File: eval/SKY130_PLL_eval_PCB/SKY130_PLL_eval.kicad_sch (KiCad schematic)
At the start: 0 parts

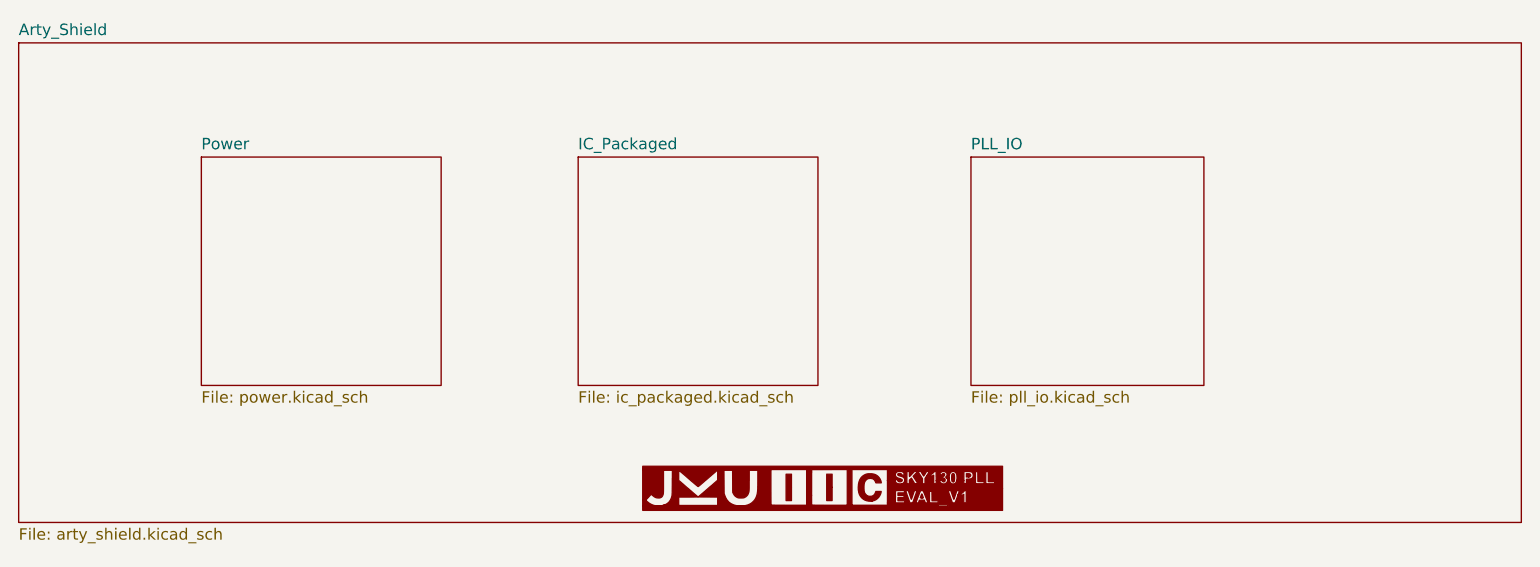
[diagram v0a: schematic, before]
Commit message: eval pcb added
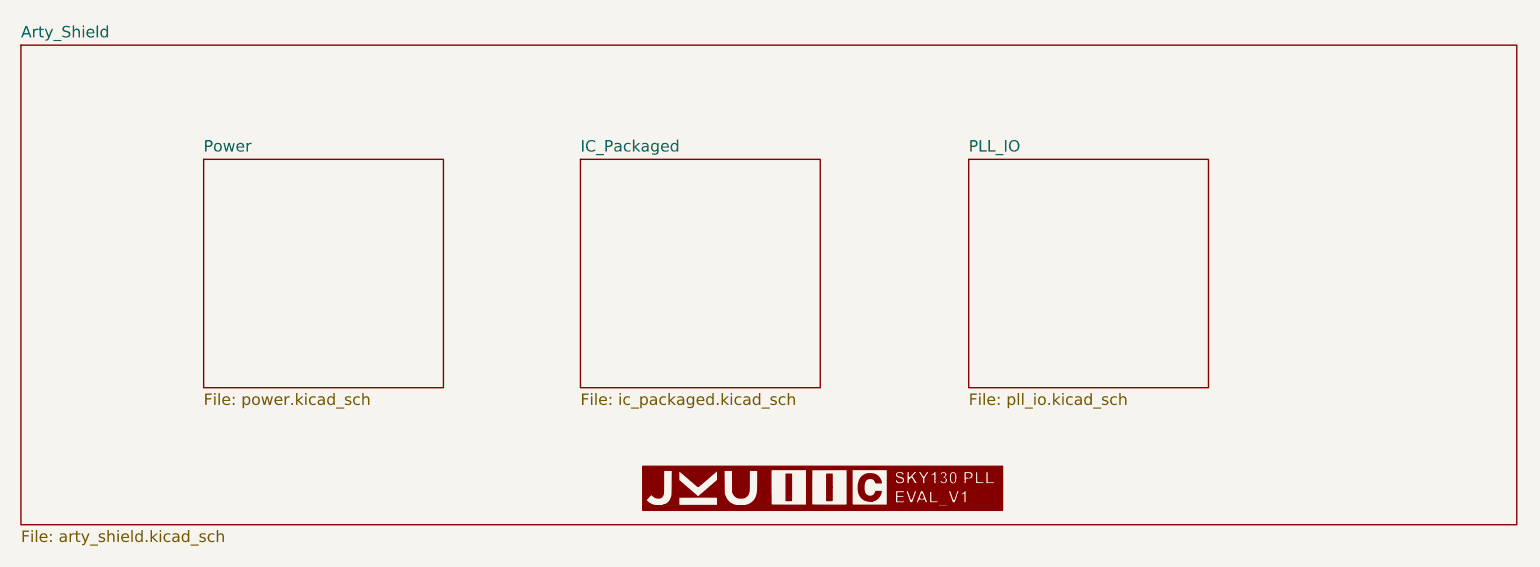
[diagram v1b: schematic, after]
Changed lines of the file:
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@@
     )
   )
-  (sheet (at 112.776 78.486) (size 26.67 25.4) (fields_autoplaced)
+  (sheet (at 113.03 78.74) (size 26.67 25.4) (fields_autoplaced)
     (stroke (width 0.1524) (type solid))
     (fill (color 0 0 0 0.0000))
-    (property "Sheetname" "Power" (at 112.776 77.7744 0)
+    (property "Sheetname" "Power" (at 113.03 78.0284 0)
       (effects (font (size 1.27 1.27)) (justify left bottom))
     )
-    (property "Sheetfile" "power.kicad_sch" (at 112.776 104.4706 0)
+    (property "Sheetfile" "power.kicad_sch" (at 113.03 104.7246 0)
       (effects (font (size 1.27 1.27)) (justify left top))
     )
@@
     )
   )
-  (sheet (at 92.456 65.786) (size 167.132 53.34) (fields_autoplaced)
+  (sheet (at 92.71 66.04) (size 166.37 53.34) (fields_autoplaced)
     (stroke (width 0.1524) (type solid))
     (fill (color 0 0 0 0.0000))
-    (property "Sheetname" "Arty_Shield" (at 92.456 65.0744 0)
+    (property "Sheetname" "Arty_Shield" (at 92.71 65.3284 0)
       (effects (font (size 1.27 1.27)) (justify left bottom))
     )
-    (property "Sheetfile" "arty_shield.kicad_sch" (at 92.456 119.7106 0)
+    (property "Sheetfile" "arty_shield.kicad_sch" (at 92.71 119.9646 0)
       (effects (font (size 1.27 1.27)) (justify left top))
     )
@@
     )
   )
-  (sheet (at 198.374 78.486) (size 25.908 25.4) (fields_autoplaced)
+  (sheet (at 198.12 78.74) (size 26.67 25.4) (fields_autoplaced)
     (stroke (width 0.1524) (type solid))
     (fill (color 0 0 0 0.0000))
-    (property "Sheetname" "PLL_IO" (at 198.374 77.7744 0)
+    (property "Sheetname" "PLL_IO" (at 198.12 78.0284 0)
       (effects (font (size 1.27 1.27)) (justify left bottom))
     )
-    (property "Sheetfile" "pll_io.kicad_sch" (at 198.374 104.4706 0)
+    (property "Sheetfile" "pll_io.kicad_sch" (at 198.12 104.7246 0)
       (effects (font (size 1.27 1.27)) (justify left top))
     )
@@
     )
   )
-  (sheet (at 154.686 78.486) (size 26.67 25.4) (fields_autoplaced)
+  (sheet (at 154.94 78.74) (size 26.67 25.4) (fields_autoplaced)
     (stroke (width 0.1524) (type solid))
     (fill (color 0 0 0 0.0000))
-    (property "Sheetname" "IC_Packaged" (at 154.686 77.7744 0)
+    (property "Sheetname" "IC_Packaged" (at 154.94 78.0284 0)
       (effects (font (size 1.27 1.27)) (justify left bottom))
     )
-    (property "Sheetfile" "ic_packaged.kicad_sch" (at 154.686 104.4706 0)
+    (property "Sheetfile" "ic_packaged.kicad_sch" (at 154.94 104.7246 0)
       (effects (font (size 1.27 1.27)) (justify left top))
     )
